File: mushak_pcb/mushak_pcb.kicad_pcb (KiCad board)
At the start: 2 copper layers, 105 parts, among them IC1 AS5600-ASOT, IC2 AS5600-ASOT, J1 Conn_01x04_Male, J10 IR_1, J11 AS5600_1, J12 IR_2, J13 AS5600_2, J14 IR_3, J15 ToF, J16 IR_4, J17 ToF, J2 Conn_01x02_Female, J3 BLE_Conn, J4 AS5600_Left, J5 AS5600_Left, J6 IR_1, J7 IR_1, J8 IR_1, J9 IR_1, Q1 DMN3065LW-7, Q2 DMN3065LW-7, Q3 DMN3065LW-7, Q4 DMN3065LW-7, Q5 DMN3065LW-7, SW1 SW_Push, SW2 SW_Push, U2 TLV1117LV30DCYT, U3 DRV8833PW, U4 VL6180XV0NR/1, U5 MPU-6500, U6 STM32F405RGTx, Y1 25Mhz, Y2 32.769kHz

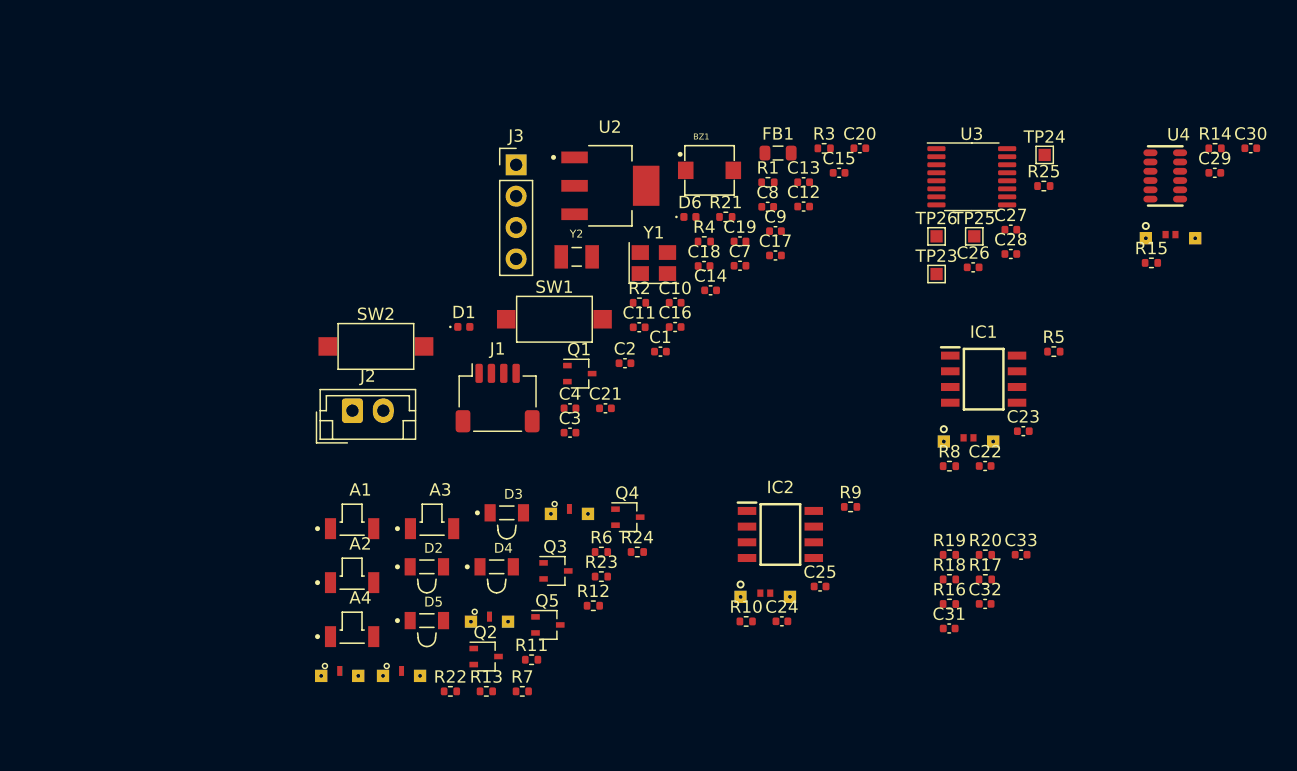
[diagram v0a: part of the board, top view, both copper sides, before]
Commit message: changed footprints of capacitors and resistors
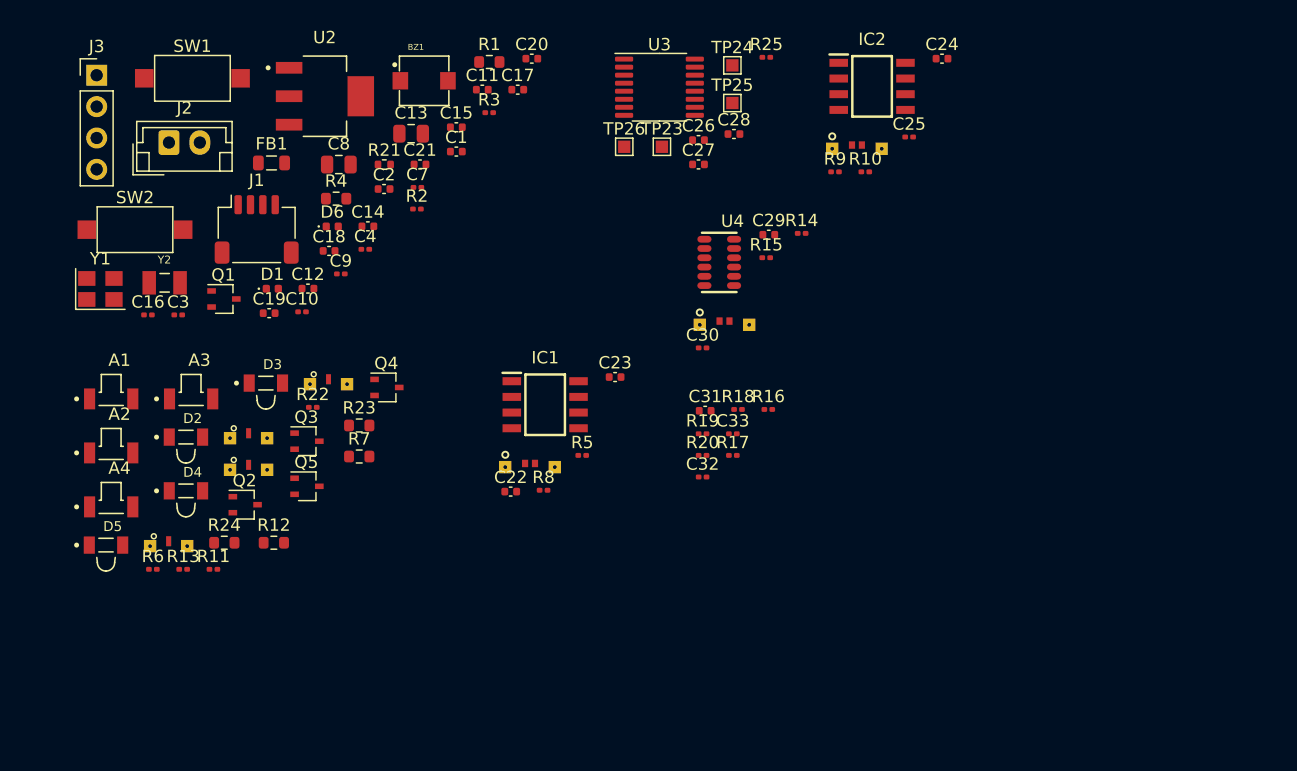
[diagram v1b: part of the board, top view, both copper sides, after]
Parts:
- C10, C16, C7, C9: value 100n -> 100nF; footprint Capacitor_SMD:C_0402_1005Metric -> Capacitor_SMD:C_0201_0603Metric
- C12, C19: value 1u -> 1uF
- C13, C8: footprint Capacitor_SMD:C_0402_1005Metric -> Capacitor_SMD:C_0805_2012Metric
- C14: value 100n -> 100nF
- C17: value 10n -> 10nF
- C18: value 10u -> 10uF
- C25, C3, C30, C32, C33, C4: footprint Capacitor_SMD:C_0402_1005Metric -> Capacitor_SMD:C_0201_0603Metric
- R1, R12, R23, R24, R4, R7: footprint Resistor_SMD:R_0402_1005Metric -> Resistor_SMD:R_0603_1608Metric
- R10, R11, R13, R14, R15, R16, R17, R18, R19, R2, R20, R22, R25, R3, R5, R6, R8, R9: footprint Resistor_SMD:R_0402_1005Metric -> Resistor_SMD:R_0201_0603Metric
- moved C24 47.3 mm to (373.2, 0.96)
- moved C30 47.2 mm to (353.9, 24.4)
- moved Y1 44.8 mm to (305.1, 19.6)
- moved C16 42.7 mm to (309.0, 21.7)
- moved FB1 41.0 mm to (319.0, 9.40)
- moved C12 40.7 mm to (321.9, 19.6)
- moved R5 39.1 mm to (344.1, 33.1)
- moved C19 38.6 mm to (318.8, 21.6)
- moved C22 38.5 mm to (338.3, 36.0)
- moved R10 37.6 mm to (367.0, 10.1)
- moved C25 37.1 mm to (370.6, 7.30)
- moved J5 37.0 mm to (366.4, 8.25)
- moved IC2 37.0 mm to (367.6, 3.20)
- moved J17 36.8 mm to (355.6, 22.5)
- moved U4 36.8 mm to (355.2, 17.5)
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
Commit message: made draft pcb footprint placement
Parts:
- added C34: 1uF, Capacitor_SMD:C_0402_1005Metric, F.Cu at (281.1, 71.2)
- added C35: 1uF, Capacitor_SMD:C_0402_1005Metric, F.Cu at (271.6, 63.3)
- added C36: 0.1uF, Capacitor_SMD:C_0201_0603Metric, F.Cu at (277.0, 67.5)
- added C37: 0.1uF, Capacitor_SMD:C_0201_0603Metric, F.Cu at (280.5, 68.5)
- added C38: 1uF, Capacitor_SMD:C_0402_1005Metric, F.Cu at (265.4, 56.8)
- added C39: 1uF, Capacitor_SMD:C_0402_1005Metric, F.Cu at (278.6, 70.2)
- added C5: 0.1uF, Capacitor_SMD:C_0201_0603Metric, F.Cu at (267.3, 57.0)
- added C6: 0.1uF, Capacitor_SMD:C_0201_0603Metric, F.Cu at (278.7, 67.5)
- added R26: 47k, Resistor_SMD:R_0201_0603Metric, F.Cu at (242.0, 50.1)
- C10, C14, C16, C23, C25, C7, C9: value 100nF -> 0.1uF
- C17, C26: value 10nF -> 0.01uF
- R11, R13, R22, R6: value 4.7k -> 10k
- U5: moved to F.Cu
- moved BZ1 198.5 mm to (163.0, 108.0), turned to 90 degrees
- moved U3 194.5 mm to (180.0, 97.0), turned to 90 degrees
- moved U2 173.5 mm to (183.0, 106.0)
- moved J1 170.0 mm to (163.0, 85.0), turned to 180 degrees
- moved Y1 163.6 mm to (167.5, 108.0), turned to 90 degrees
- moved Y2 157.5 mm to (168.5, 87.5), turned to -90 degrees
- moved SW1 153.6 mm to (186.0, 89.5), turned to 180 degrees
- moved J2 153.5 mm to (186.7, 98.2), turned to 90 degrees
- moved J3 149.8 mm to (192.0, 100.8), turned to 180 degrees
- moved SW2 140.9 mm to (186.0, 85.5), turned to 180 degrees
- moved C24 134.4 mm to (239.6, 15.4), turned to 90 degrees
- moved IC2 127.0 mm to (241.8, 21.1), turned to 90 degrees
- moved C25 125.1 mm to (245.9, 18.1), turned to 90 degrees
- moved R25 122.9 mm to (239.5, 29.6), turned to 90 degrees
- moved J5 120.3 mm to (246.9, 22.3), turned to 90 degrees
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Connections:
- D2 pad 1: Net-(D2-Pad1) -> Net-(Q2-Pad1)
- D2 pad 2: POW_IN -> Net-(D2-Pad2)
- D3 pad 2: POW_IN -> Net-(C35-Pad1)
- D4 pad 2: POW_IN -> Net-(C38-Pad1)
- D5 pad 2: POW_IN -> Net-(C39-Pad1)
- Q3 pad 1: Net-(Q3-Pad1) -> Net-(D3-Pad1)
- Q4 pad 1: Net-(Q4-Pad1) -> Net-(D4-Pad1)
- Q5 pad 1: Net-(Q5-Pad1) -> Net-(D5-Pad1)
- R12 pad 1: Net-(D3-Pad1) -> POW_IN
- R12 pad 2: Net-(Q3-Pad1) -> Net-(C35-Pad1)
- R23 pad 1: Net-(D4-Pad1) -> POW_IN
- R23 pad 2: Net-(Q4-Pad1) -> Net-(C38-Pad1)
- R24 pad 1: Net-(D5-Pad1) -> POW_IN
- R24 pad 2: Net-(Q5-Pad1) -> Net-(C39-Pad1)
- R7 pad 1: Net-(D2-Pad1) -> POW_IN
- R7 pad 2: Net-(Q2-Pad1) -> Net-(D2-Pad2)
- U6 pad 60: POW_GND -> Net-(U6-Pad60)
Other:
- board outline added: 45.8 x 40 mm

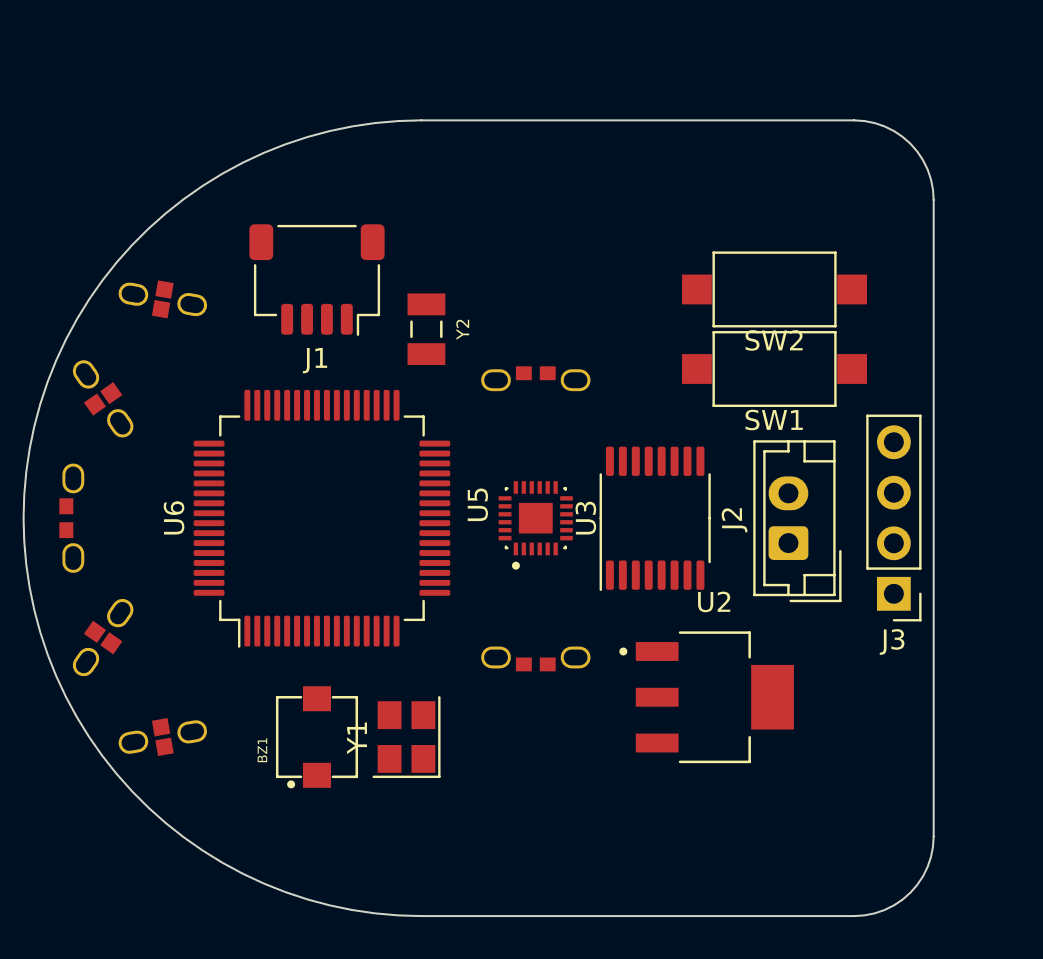
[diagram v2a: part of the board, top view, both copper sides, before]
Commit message: Add 3d models to footprint
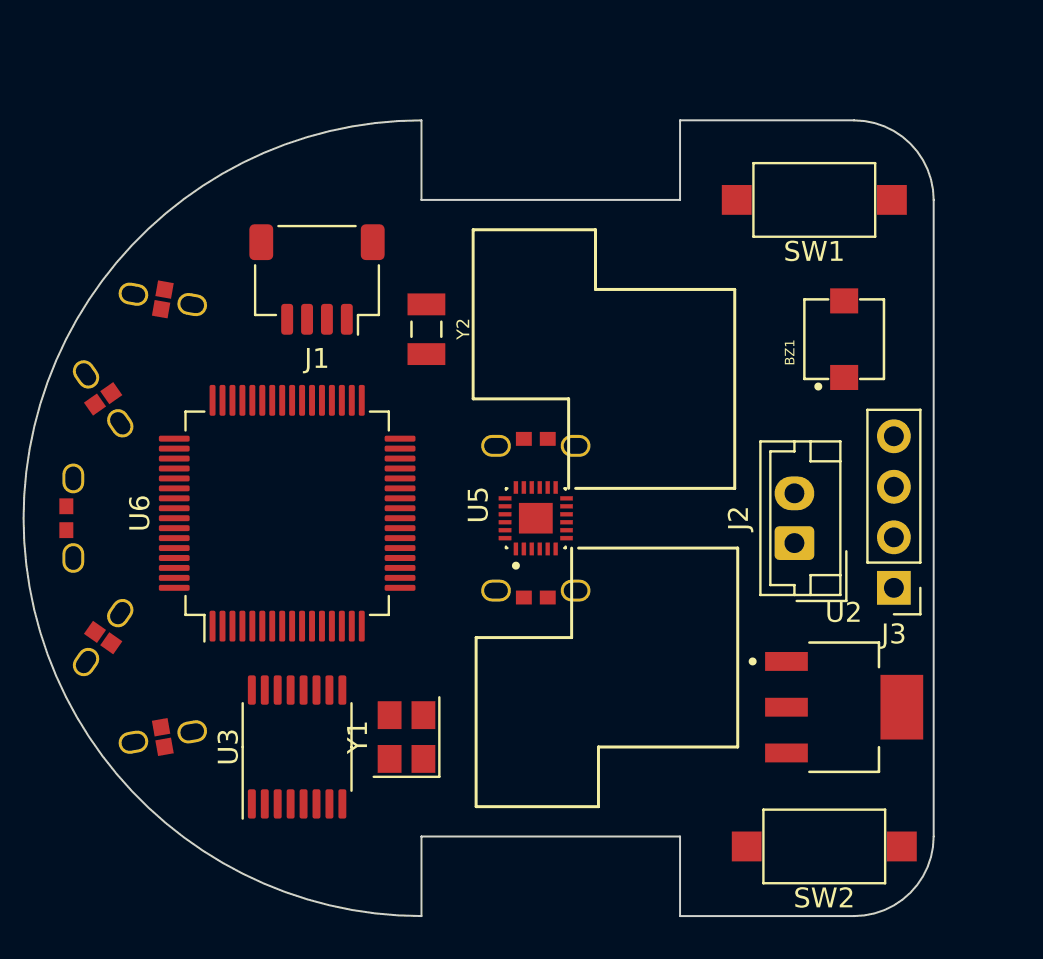
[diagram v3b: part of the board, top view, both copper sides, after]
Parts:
- moved BZ1 33.2 mm to (189.5, 88.0)
- moved SW2 28.1 mm to (188.5, 113.5)
- moved U3 21.4 mm to (162.0, 108.5)
- moved SW1 8.73 mm to (188.0, 81.0)
- moved U2 6.52 mm to (189.5, 106.5)
- moved J13 3.36 mm to (174.0, 100.6)
- moved J11 3.30 mm to (174.0, 93.4)
- moved U6 1.77 mm to (161.5, 96.8)
- moved J2 0.30 mm to (187.0, 98.2)
- moved J3 0.30 mm to (192.0, 100.5)
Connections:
- C20 pad 1: Net-(C20-Pad1) -> Net-(U6-Pad3)
- C21 pad 1: Net-(C21-Pad1) -> Net-(U6-Pad4)
- U6 pad 16: IR_RES_2 -> RXD
- U6 pad 17: IR_RES_3 -> TXD
- U6 pad 2: IR_LED_2 -> unconnected-(U6-Pad2)
- U6 pad 20: IR_RES_4 -> IR_RES_2
- U6 pad 21: /MPU6500/SCLK -> IR_RES_3
- U6 pad 22: /MPU6500/MISO -> /DRV8833_Motor_Driver/BIN2
- U6 pad 23: /MPU6500/MOSI -> IR_RES_4
- U6 pad 24: BUZZER_OP -> unconnected-(U6-Pad24)
- U6 pad 26: DEBUG -> /DRV8833_Motor_Driver/AIN2
- U6 pad 27: /DRV8833_Motor_Driver/EN -> /DRV8833_Motor_Driver/BIN1
- U6 pad 28: /DRV8833_Motor_Driver/BIN2 -> unconnected-(U6-Pad28)
- U6 pad 3: IR_LED_3 -> Net-(U6-Pad3)
- U6 pad 35: Net-(C21-Pad1) -> IR_LED_4
- U6 pad 36: Net-(C20-Pad1) -> IR_LED_3
- U6 pad 37: unconnected-(U6-Pad37) -> IR_LED_1
- U6 pad 38: unconnected-(U6-Pad38) -> IR_LED_2
- U6 pad 4: IR_LED_4 -> Net-(U6-Pad4)
- U6 pad 42: /MPU6500/nCS -> unconnected-(U6-Pad42)
- U6 pad 43: unconnected-(U6-Pad43) -> DEB_LED
- U6 pad 44: unconnected-(U6-Pad44) -> /MPU6500/nCS
- U6 pad 45: unconnected-(U6-Pad45) -> DEBUG
- U6 pad 50: DEB_LED -> unconnected-(U6-Pad50)
- U6 pad 51: RXD -> unconnected-(U6-Pad51)
- U6 pad 52: TXD -> unconnected-(U6-Pad52)
- U6 pad 53: IR_LED_1 -> unconnected-(U6-Pad53)
- U6 pad 55: /DRV8833_Motor_Driver/AIN2 -> /MPU6500/SCLK
- U6 pad 56: /DRV8833_Motor_Driver/BIN1 -> /MPU6500/MISO
- U6 pad 57: /DRV8833_Motor_Driver/AIN1 -> /MPU6500/MOSI
- U6 pad 61: unconnected-(U6-Pad61) -> /DRV8833_Motor_Driver/AIN1
- U6 pad 62: unconnected-(U6-Pad62) -> BUZZER_OP
- Y2 pad 1: Net-(C20-Pad1) -> Net-(U6-Pad3)
- Y2 pad 2: Net-(C21-Pad1) -> Net-(U6-Pad4)
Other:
- outline, holes or cut-outs redrawn

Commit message: updated footprint for motors
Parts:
- removed C22, C24: 10uF, Capacitor_SMD:C_0402_1005Metric
- removed TP23, TP24: MOT_1, TestPoint:TestPoint_Pad_1.0x1.0mm
- removed TP25, TP26: MOT_2, TestPoint:TestPoint_Pad_1.0x1.0mm
- added M1: motor, mushak_mount_footprint:motor, F.Cu at (170.5, 112.9)
- added M2: motor, mushak_mount_footprint:motor, B.Cu at (170.5, 81.2)
- SW1, SW2: footprint Button_Switch_SMD:SW_SPST_CK_RS282G05A3 -> TL1015AF160QG:SW_TL1015AF160QG
- moved D5 278.2 mm to (20.1, 184.8), turned to 0 degrees
- moved A3 274.0 mm to (20.5, 181.7), turned to 0 degrees
- moved R12 273.6 mm to (31.0, 188.9), turned to 0 degrees
- moved R24 271.6 mm to (35.0, 188.9), turned to 0 degrees
- moved J9 270.4 mm to (31.5, 186.6), turned to 0 degrees
- moved C34 269.6 mm to (38.4, 188.6), turned to 0 degrees
- moved A4 268.3 mm to (20.5, 177.4), turned to 0 degrees
- moved R7 267.8 mm to (36.0, 186.4), turned to 0 degrees
- moved C37 267.6 mm to (41.1, 188.0), turned to 0 degrees
- moved C39 265.8 mm to (39.4, 186.1), turned to 0 degrees
- moved C6 264.8 mm to (42.1, 186.2), turned to 0 degrees
- moved D2 263.8 mm to (32.9, 182.2), turned to 0 degrees
- moved Q3 262.9 mm to (37.7, 183.3), turned to 0 degrees
- moved A1 262.7 mm to (20.5, 173.0), turned to 0 degrees
- moved C36 262.4 mm to (42.1, 184.5), turned to 0 degrees
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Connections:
- IC2 pad 8: /AS5600_Right/+3V0 -> /AS5600_Right/GND
- U6 pad 28: unconnected-(U6-Pad28) -> /DRV8833_Motor_Driver/EN
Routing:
- net POW_GND: track 0.00 -> 5.07 mm
- net BAT_VOL: track 0.00 -> 3.68 mm
- net +3V0: track 0.00 -> 2.97 mm
- net Net-(BZ1-Pad2): track 0.00 -> 1.92 mm
- net POW_IN: track 0.00 -> 1.87 mm
- net Net-(C26-Pad2): track 0.00 -> 1.41 mm
- net Net-(C27-Pad2): track 0.00 -> 1.39 mm
- net Net-(C1-Pad1): track 0.00 -> 1.36 mm
- net Net-(C21-Pad1): track 0.00 -> 1.27 mm
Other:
- copper layers 2 -> 4

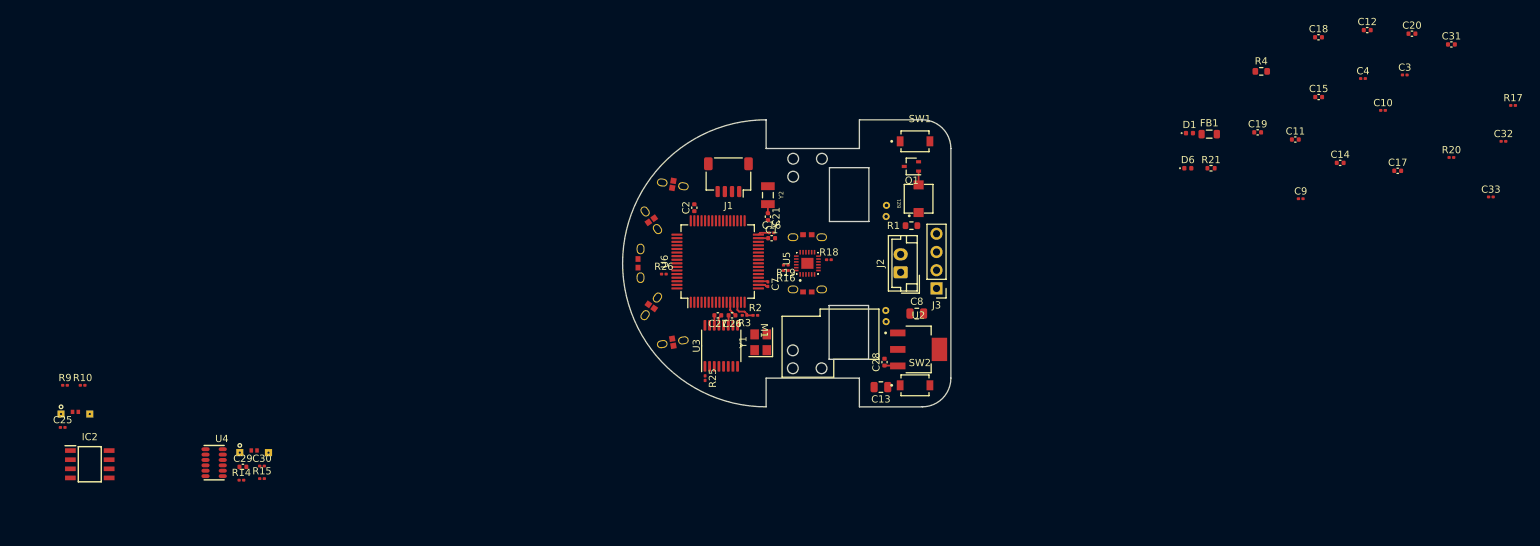
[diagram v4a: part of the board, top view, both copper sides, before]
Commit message: corrected encoder and motor driver schematics
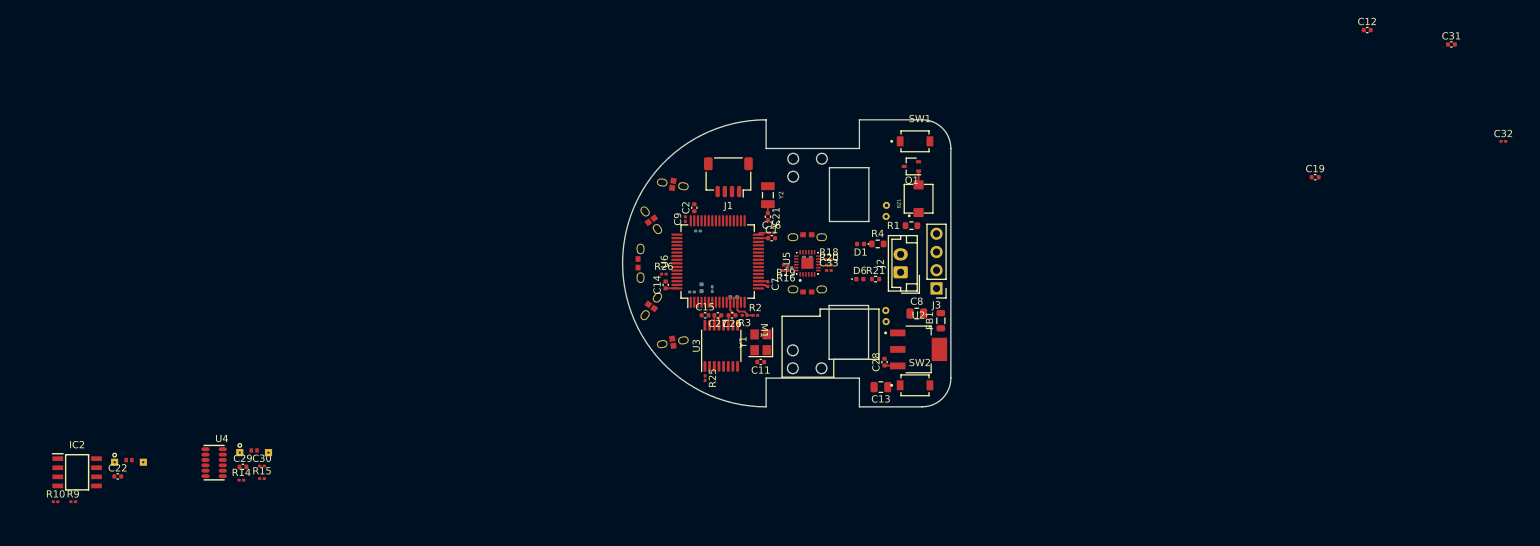
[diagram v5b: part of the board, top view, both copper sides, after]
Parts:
- removed C25: 0.1uF, Capacitor_SMD:C_0201_0603Metric
- added C22: 0.1uF, Capacitor_SMD:C_0402_1005Metric, F.Cu at (77.9, 126.7)
- C10, C17, C18, C20, C3, C4, R17: moved to B.Cu
- J5: value AS5600_Left -> AS5600_Right
- J7: value IR_1 -> IR_3
- J8: value IR_1 -> IR_2
- J9: value IR_1 -> IR_4
- moved C20 105.1 mm to (159.2, 100.4), turned to 90 degrees
- moved R17 103.3 mm to (171.5, 97.6), turned to 180 degrees
- moved C3 101.0 mm to (160.8, 100.6), turned to 90 degrees
- moved C10 99.6 mm to (157.9, 101.0)
- moved C14 95.5 mm to (154.2, 100.0), turned to 90 degrees
- moved C4 95.1 mm to (158.8, 92.5), turned to 180 degrees
- moved C17 94.2 mm to (163.8, 101.8), turned to 180 degrees
- moved C33 92.8 mm to (177.0, 98.0)
- moved C15 90.8 mm to (159.8, 104.2)
- moved R20 88.0 mm to (177.0, 97.2)
- moved C9 85.8 mm to (157.0, 90.8), turned to 90 degrees
- moved C11 80.7 mm to (167.5, 110.8), turned to 180 degrees
- moved C18 77.6 mm to (174.0, 96.2), turned to 180 degrees
- moved R4 58.6 mm to (183.8, 94.3)
- moved R21 49.2 mm to (183.5, 99.2)
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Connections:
- net /AS5600_Right/+3V0 renamed /AS5600_Right/+3V0_s
- net /AS5600_Right/GND renamed /AS5600_Right/GND_s
- net /AS5600_Right/SCL renamed /AS5600_Right/SCL_s
- net /AS5600_Right/SDA renamed /AS5600_Right/SDA_s
- net /VL6180x/GND renamed /VL6180x/GND_s
- C23 pad 1: /AS5600_Left/+3V0 -> /AS5600_Left/GND_s
- C23 pad 2: /AS5600_Left/GND -> /AS5600_Left/+3V0_s
- C26 pad 1: POW_GND -> POW_IN
- C29 pad 1: /VL6180x/3V0 -> /VL6180x/3V0_s
- C30 pad 1: /VL6180x/3V0 -> /VL6180x/3V0_s
- IC1 pad 1: /AS5600_Left/+3V0 -> /AS5600_Left/+3V0_s
- IC1 pad 2: /AS5600_Left/+3V0 -> /AS5600_Left/+3V0_s
- IC1 pad 4: /AS5600_Left/GND -> /AS5600_Left/GND_s
- IC1 pad 6: /AS5600_Left/SDA -> /AS5600_Left/SDA_s
- IC1 pad 7: /AS5600_Left/SCL -> /AS5600_Left/SCL_s
- IC1 pad 8: /AS5600_Left/+3V0 -> /AS5600_Left/+3V0_s
- J17 pad 1: /VL6180x/3V0 -> /VL6180x/3V0_s
- J17 pad 2: /VL6180x/SDA -> /VL6180x/SDA_s
- J17 pad 3: /VL6180x/SCL -> /VL6180x/SCL_s
- J4 pad 1: /AS5600_Left/+3V0 -> /AS5600_Left/+3V0_s
- J4 pad 2: /AS5600_Left/SDA -> /AS5600_Left/SDA_s
- J4 pad 3: /AS5600_Left/SCL -> /AS5600_Left/SCL_s
- J4 pad 4: /AS5600_Left/GND -> /AS5600_Left/GND_s
- R14 pad 1: /VL6180x/SCL -> /VL6180x/SDA_s
- R14 pad 2: /VL6180x/3V0 -> /VL6180x/3V0_s
- R15 pad 1: /VL6180x/SDA -> /VL6180x/SDA_s
- R15 pad 2: /VL6180x/3V0 -> /VL6180x/3V0_s
- R5 pad 1: /AS5600_Left/+3V0 -> /AS5600_Left/+3V0_s
- R5 pad 2: /AS5600_Left/SCL -> /AS5600_Left/SDA_s
- R8 pad 1: /AS5600_Left/+3V0 -> /AS5600_Left/+3V0_s
- R8 pad 2: /AS5600_Left/SDA -> /AS5600_Left/SCL_s
- U4 pad 10: /VL6180x/3V0 -> /VL6180x/3V0_s
- U4 pad 4: /VL6180x/3V0 -> Net-(U4-Pad4)
- U4 pad 5: /VL6180x/SCL -> /VL6180x/SDA_s
- U4 pad 6: /VL6180x/SDA -> /VL6180x/SDA_s
- U4 pad 8: /VL6180x/3V0 -> /VL6180x/3V0_s
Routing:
- net +3V0: track 2.97 -> 4.55 mm
